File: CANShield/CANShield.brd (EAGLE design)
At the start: 53.3 x 61 mm, 31 parts, among them Q1 16MHz, U2 ARDUINO_R3_SHIELD, U4 MCP2515, U5 MCP2551, X1 DB9 Plug

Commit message: Can shield
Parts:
- removed C7: 22pF, SparkFun-Capacitors:0603-CAP
- removed CONTACTOR, CONTACTOR2, LEDS, PACKV: MSTBA2, con-phoenix-508:MSTBA2
- removed D3, D7: BAS40-04, diode:SOT23
- removed F2: PTCTHERMISTOR1206, SparkFun-PowerIC:PTC-1206
- removed S2: RESET, SparkFun-Electromechanical:TACTILE-SWITCH-SMD
- removed U2: ARDUINO_R3_SHIELD, SparkFun-Boards:UNO_R3_SHIELD
- removed U4: MCP2515, SparkFun-DigitalIC:SO-18W
- added F3: 1812L, ptc-littlefuse:1812L
- added FANS, ON: MSTBA3, con-phoenix-508:MSTBA3
- added FAN_LEDS, GAUGES_APA102, PACK_LEDS: MSTBA4, con-phoenix-508:MSTBA4
- added IC1: 7805DT, linear:TO252
- added IC2: 74LVC2G125DCT, 74xx-little-de:SSOP08
- added J2: POWERPOLE_POWER25A_HORIZONTAL_G2, powerpoles:POWERPOLE_PAIR_25A_HORIZ_G2
- added PRECHG1, PRECHG2: (no value), SparkFun-Connectors:MOLEX-1X6
- added Q2, Q3, Q4, Q5, Q6: MOSFET-NCHANNELFDD8780, SparkFun-DiscreteSemi:DPAK
- added Q7: MOSFET-NCHANNELBSS123LT1G, SparkFun-DiscreteSemi:SOT23-3
- added Q8: BSS123, transistor-small-signal:SOT23
- added R11, R15, R17, R19, R21, R23, R24, R25, R26, R27, R28, R8: 10K, SparkFun-Resistors:0603-RES
- added R14, R16, R18, R20, R6, R7, R9: 100R, SparkFun-Resistors:0603-RES
- added R22, R31, R32: (no value), SparkFun-Passives:0603-RES
- added R29: 100R, SparkFun-Passives:0603-RES
- added R30: 10K, SparkFun-Passives:0603-RES
- added R4: 100K, SparkFun-Resistors:0603-RES
- added SBO_1, SBO_2: (no value), adafruit:JST-PH-2-THM-RA
- added SG1: BUZZERNS, SparkFun-Electromechanical:BUZZER-12MM-NS
- added U$1: TEENSY_3.0_BASIC-PGM, Teensy3.0:TEENSY_3.0_BASIC-PGM
- added U$2: F6136TR-ND, ptc-littlefuse:1812L
- C1: value 0.1uF -> (none); device SparkFun-Capacitors:0603-CAP -> SparkFun-Capacitors:EIA3216
- C4: value 4.7uF -> (none); device SparkFun-Capacitors:0603-CAP -> SparkFun-Capacitors:EIA3216
- C5: value 22pF -> (none)
- D1: value MBRA140 -> (none); device SparkFun-DiscreteSemi:SMA-DIODE -> SparkFun-LED:LED-1206
- D2: value BAS40-04 -> 250mA/100V; device diode:SOT23 -> SparkFun-DiscreteSemi:SOD-323
- D5: device SparkFun-DiscreteSemi:SOT23-3 -> SparkFun-DiscreteSemi:SOT23-3@1
- F1: value (none) -> 1812L; device SparkFun-PowerIC:PTC-1206 -> ptc-littlefuse:1812L
- Q1: value 16MHz -> MOSFET-NCHANNELFDD8780; device SparkFun-FreqCtrl:CRYSTAL-SMD-5X3 -> SparkFun-DiscreteSemi:DPAK
- R1, R5: value (none) -> 10K
- R2: value 100R -> 100K
- moved D2 290.0 mm to (-132.1, -224.8), turned to 0 degrees
- moved C5 276.8 mm to (-128.3, -213.4), turned to 0 degrees
- moved D1 222.2 mm to (-90.2, -144.8), turned to 0 degrees
- moved C4 128.7 mm to (-61.0, -52.1), turned to 0 degrees
- moved C1 122.6 mm to (-62.2, -54.6), turned to 0 degrees
- moved Q1 61.3 mm to (71.1, 27.9)
- moved C3 57.2 mm to (23.5, 103.5)
- moved R12 57.2 mm to (23.5, 100.3)
- moved X1 57.2 mm to (26.7, 108.0)
- moved C2 57.1 mm to (24.8, 94.5)
- moved C6 57.1 mm to (23.7, 92.2)
- moved D5 57.1 mm to (19.1, 98.8)
- moved R1 57.1 mm to (27.9, 68.6)
- moved R10 57.1 mm to (24.8, 96.5)
- moved R13 57.1 mm to (14.6, 91.4)
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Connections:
- removed net 12V: C4.1, D1.C, U2.VIN
- removed net A0: D7.3, R2.1, U2.A0
- removed net AREF: U2.AREF
- removed net CAN_CS: U2.D10, U4.16
- removed net CAN_INT: U2.D2, U4.12
- removed net CONTACT_SENSE_1: CONTACTOR2.1, D3.3, R5.2, U2.D9
- removed net CONTACT_SENSE_2: CONTACTOR.1, D2.3, R1.2, U2.D8
- removed net D3: U2.D3
- removed net D4: U2.D4
- removed net D5: U2.D5
- removed net MISO: U2.D12, U4.15
- removed net MOSI: U2.D11, U4.14
- removed net RS: S2.3, U2.RES, U4.17
- removed net RX: U2.RX
- removed net SCK: U2.D13, U4.13
- removed net TX: U2.TX
- new net +12V: F1.2, F3.2, FANS.1, J2.RED, ON.1, PRECHG1.2, PRECHG2.2, U$2.1
- new net +5V: C1.A, C5.1, C6.2, D2.C, IC1.2, IC2.8, R22.2, SG1.+, U$1.VIN, U5.3
- new net ACTIVE_1: PRECHG1.4, R24.1, U$1.17/A3
- new net ACTIVE_2: PRECHG2.4, R27.1, U$1.14/A0
- new net BUZZER: R29.1, U$1.20/A6
- new net CHARGED_1: PRECHG1.5, R25.1, U$1.18/A4
- new net CHARGED_2: PRECHG2.5, R28.1, U$1.15/A1
- new net CHARGING_1: PRECHG1.6, R23.1, U$1.19/A5
- new net CHARGING_2: PRECHG2.6, R26.1, U$1.16/A2
- new net FANS_B: R20.1, U$1.9
- new net FANS_G: R18.1, U$1.6
- new net FANS_R: R16.1, U$1.5
- new net FAN_PWM: R31.1, U$1.10
- new net LED_C: IC2.5, U$1.13
- new net N$11: PACK_LEDS.4, Q3.4
- new net N$12: Q1.1, R7.2, R8.2
- new net N$15: Q3.1, R14.2, R15.2
- new net N$19: F3.1, FAN_LEDS.1
- new net N$20: FAN_LEDS.2, Q4.4
- new net N$21: FAN_LEDS.3, Q5.4
- new net N$22: FAN_LEDS.4, Q6.4
- new net N$23: Q4.1, R16.2, R17.2
- new net N$24: Q5.1, R18.2, R19.2
- new net N$25: Q6.1, R20.2, R21.2
- new net N$26: Q7.1, R29.2, R30.2
- new net N$27: Q8.1, R31.2, R32.2
- new net N$28: FANS.3, Q8.3
- new net N$29: GAUGES_APA102.1, U$2.2
- new net N$4: R4.2, SBO_2.1
- new net N$5: GAUGES_APA102.4, R6.1
- new net N$6: PACK_LEDS.2, Q1.4
- new net N$7: F1.1, PACK_LEDS.1
- new net N$8: PACK_LEDS.3, Q2.4
- new net PACK_B: R14.1, U$1.23/A9
- new net PACK_G: R9.1, U$1.22/A8
- new net PACK_R: R7.1, U$1.21/A7
- new net SBO_SENSE_1: R1.2, R4.1, U$1.7
- new net SBO_SENSE_2: R2.1, R5.2, U$1.8
- new net VBAT: U$1.VBAT
- new net VCC: C4.A, IC1.1, ON.2
- net 3.3V: now also U$1.3.3V, U$1.3.3V1; no longer U2.3.3V
- net 5V: now also PRECHG1.3, PRECHG2.3, R1.1, R23.2, R24.2, R25.2, R26.2, R27.2, R28.2, R5.1; no longer C1.2, C6.2, D2.2, D3.2, D7.2, F2.2, U2.5V, U4.18, U5.3
- net CAN_RXD: now also U$1.4; no longer U4.2
- net CAN_TXD: now also U$1.3; no longer U4.1
- net GND: now also C1.C, C4.C, C5.2, D1.C, FANS.2, GAUGES_APA102.2, IC1.3, IC2.1, IC2.4, IC2.7, J2.BLACK, ON.3, PRECHG1.1, PRECHG2.1, Q1.3, Q2.3, Q3.3, Q4.3, Q5.3, Q6.3, Q7.2, Q8.2, R11.1, R15.1, R17.1, R19.1, R21.1, R30.1, R32.1, R8.1, U$1.AGND, U$1.GND, U$1.GND1; no longer C1.1, C4.2, C5.1, C7.1, D2.1, D3.1, D7.1, LEDS.1, PACKV.2, R1.1, R5.1, S2.1, U2.GND@0, U2.GND@1, U2.GND@2, U4.9
- net LED_D: now also IC2.2, U$1.11; no longer R3.2, U2.SDA
- net N$1: now also SBO_1.1; no longer PACKV.1
- net N$13: now also Q2.1, R11.2, R9.2; no longer F1.2, X1.9
- net N$16: now also R22.1; no longer F1.1
- net N$17: now also IC2.6, R3.2; no longer C7.2, Q1.3, U4.8
- net N$18: now also D2.A, Q7.3, SG1.-; no longer C5.2, Q1.1, U4.7
- net N$2: now also IC2.3, R6.2; no longer CONTACTOR.2, CONTACTOR2.2, F2.1
- net N$3: now also GAUGES_APA102.3; no longer LEDS.2
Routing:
- net 5V: track 81.8 -> 0.00 mm, vias 2 -> 0
- net PACK_R: track 0.00 -> 56.9 mm
- net CONTACT_SENSE_2: track 54.5 -> 0.00 mm
- net PACK_G: track 0.00 -> 47.0 mm
- net CAN_INT: track 45.1 -> 0.00 mm, vias 1 -> 0
- net CAN_TXD: track 6.24 -> 49.7 mm
- net CONTACT_SENSE_1: track 39.5 -> 0.00 mm
- net PACK_B: track 0.00 -> 38.1 mm
- net A0: track 31.6 -> 0.00 mm, vias 1 -> 0
- net RS: track 29.7 -> 0.00 mm, vias 1 -> 0
- net CAN_RXD: track 11.3 -> 40.3 mm
- net N$2: track 23.1 -> 0.00 mm
- net SCK: track 22.4 -> 0.00 mm, vias 1 -> 0
- net MISO: track 22.4 -> 0.00 mm, vias 1 -> 0
- net MOSI: track 21.8 -> 0.00 mm, vias 1 -> 0
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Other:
- board size 53.3 x 61 mm -> 88.9 x 116.8 mm
- board text removed: "Units: inches"

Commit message: Most of the base board finished
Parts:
- removed PRECHG1, PRECHG2: (no value), SparkFun-Connectors:MOLEX-1X6
- removed R23, R24, R25, R26, R27, R28: 10K, SparkFun-Resistors:0603-RES
- removed SBO_1, SBO_2: (no value), adafruit:JST-PH-2-THM-RA
- added D3, D4: BAS40-04, diode:SOT23
- added H1, H2, H3, H4: MOUNT-PAD-ROUND3.0, holes:3,0-PAD
- added IC3, IC4, IC5: ILD213T, SparkFun-DiscreteSemi:SO08
- added SBO_LOOP_1, SBO_LOOP_2: MSTBA2, con-phoenix-508:MSTBA2
- C1, C4: device SparkFun-Capacitors:EIA3216 -> SparkFun-Capacitors:PANASONIC_C
- moved R32 386.9 mm to (69.8, 82.5)
- moved R31 386.9 mm to (69.8, 85.1)
- moved Q8 384.7 mm to (74.9, 85.1), turned to 270 degrees
- moved D2 360.7 mm to (64.8, 77.5), turned to 270 degrees
- moved R29 359.1 mm to (61.8, 71.1)
- moved R30 359.1 mm to (61.8, 68.6)
- moved Q7 358.2 mm to (66.0, 71.1), turned to 270 degrees
- moved SG1 355.1 mm to (72.4, 75.4)
- moved C5 341.9 mm to (72.4, 63.5)
- moved R22 303.8 mm to (91.4, 95.2), turned to 180 degrees
- moved D1 302.5 mm to (88.9, 99.1)
- moved R21 223.8 mm to (61.0, 22.9)
- moved C1 213.9 mm to (83.8, 101.6), turned to 180 degrees
- moved IC1 206.9 mm to (76.2, 109.2)
- moved C4 204.9 mm to (68.6, 106.7)
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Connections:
- net +12V: no longer PRECHG1.2, PRECHG2.2
- net +5V: now also C1.+; no longer C1.A
- net 5V: now also D3.2, D4.2; no longer PRECHG1.3, PRECHG2.3, R23.2, R24.2, R25.2, R26.2, R27.2, R28.2
- net ACTIVE_1: no longer PRECHG1.4, R24.1
- net ACTIVE_2: no longer PRECHG2.4, R27.1
- net BUZZER: now also U$1.23/A9; no longer U$1.20/A6
- net CHARGED_1: no longer PRECHG1.5, R25.1
- net CHARGED_2: no longer PRECHG2.5, R28.1
- net CHARGING_1: no longer PRECHG1.6, R23.1
- net CHARGING_2: no longer PRECHG2.6, R26.1
- net FANS_B: now also U$1.5; no longer U$1.9
- net FANS_R: now also U$1.9; no longer U$1.5
- net GND: now also C1.-, C4.-, D3.1, D4.1, H1.B3,0, H2.B3,0, H3.B3,0, H4.B3,0, SBO_LOOP_1.2, SBO_LOOP_2.2; no longer C1.C, C4.C, PRECHG1.1, PRECHG2.1
- net N$1: now also SBO_LOOP_2.1; no longer SBO_1.1
- net N$4: now also SBO_LOOP_1.1; no longer SBO_2.1
- net PACK_B: now also U$1.22/A8; no longer U$1.23/A9
- net PACK_G: now also U$1.21/A7; no longer U$1.22/A8
- net PACK_R: now also U$1.20/A6; no longer U$1.21/A7
- net SBO_SENSE_1: now also D3.3
- net SBO_SENSE_2: now also D4.3
- net VCC: now also C4.+; no longer C4.A
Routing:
- net +5V: track 0.00 -> 137.1 mm
- net FANS_R: track 0.00 -> 105.7 mm, vias 0 -> 1
- net FANS_G: track 0.00 -> 96.0 mm, vias 0 -> 1
- net FANS_B: track 0.00 -> 85.1 mm, vias 0 -> 1
- net LED_D: track 0.00 -> 72.6 mm, vias 0 -> 1
- net LED_C: track 0.00 -> 57.3 mm, vias 0 -> 1
- net CHARGING_1: track 0.00 -> 29.8 mm
- net VCC: track 0.00 -> 28.6 mm
- net CHARGED_1: track 0.00 -> 26.8 mm
- net ACTIVE_1: track 0.00 -> 23.7 mm
- net +12V: track 0.00 -> 21.4 mm
- net CHARGING_2: track 0.00 -> 20.6 mm
- net CHARGED_2: track 0.00 -> 17.6 mm
- net BUZZER: track 0.00 -> 17.1 mm
- net SBO_SENSE_1: track 0.00 -> 16.4 mm
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- added copper zone on layer 16, net +12V
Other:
- board size 88.9 x 116.8 mm -> 96.5 x 128.3 mm
- board text removed: "RESET"

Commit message: precharge progress
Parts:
- removed IC4, IC5: ILD213T, SparkFun-DiscreteSemi:SO08
- added 74HC125M: MM74HC125M, Fairchild_By_element14_Batch_1:SOIC127P600X175-14N
- added D10, D11, D6, D7: (no value), SparkFun-DiscreteSemi:SOD-123
- added LM393M: LM393M, Fairchild_By_element14_Batch_1:SOIC127P600X180-8N
- added PRECHARGE_FUSE: FUSEX20MM, SparkFun-Passives:FUSE_5MM
- added PRECHARGE_RELAY, PRECHARGE_RELAY1: DS2Y-S-DC5V, relay:DS2Y
- added Q11, Q13, Q14, Q9: IRLML6344TRPBF, SparkFun-DiscreteSemi:SOT23
- added R23, R24, R25, R26: 10K, SparkFun-Passives:0603-RES
- added R33, R45: 100k, SparkFun-Resistors:0603-RES
- added R34, R41, R46, R47: 10k, SparkFun-Resistors:0603-RES
- added R36, R37, R42: 470k, SparkFun-Resistors:0805
- added R38, R43: 13K, SparkFun-Resistors:0805
- added R39: 110k, SparkFun-Resistors:0805
- added R40: 12K, SparkFun-Resistors:0805
- added U$4: (no value), prosthesis:PROS_LOGO
- added U$5: REE-0505S, grant:REE-0505S
- added U$7, U$8: RELAY-2G5Q, SparkFun-Electromechanical:RELAY-G5V
- added X2, X3, X4, X5: SMKDSP_1,5/2, con-phoenix-smkdsp:SMKDSP_1,5/2
- FANS, ON: value MSTBA3 -> SMKDSP_1,5/3; device con-phoenix-508:MSTBA3 -> con-phoenix-smkdsp:SMKDSP_1,5/3
- FAN_LEDS, GAUGES_APA102, PACK_LEDS: value MSTBA4 -> SMKDSP_1,5/4; device con-phoenix-508:MSTBA4 -> con-phoenix-smkdsp:SMKDSP_1,5/4
- Q7: device SparkFun-DiscreteSemi:SOT23-3 -> SparkFun-DiscreteSemi:SOT23
- R10, R12, R13: device SparkFun-Resistors:0603-RES -> SparkFun-Resistors:0603-RES@1
- SBO_LOOP_1, SBO_LOOP_2: value MSTBA2 -> SMKDSP_1,5/2; device con-phoenix-508:MSTBA2 -> con-phoenix-smkdsp:SMKDSP_1,5/2
- moved Q7 46.0 mm to (44.5, 111.8), turned to 0 degrees
- moved R30 45.3 mm to (41.1, 108.8), turned to 270 degrees
- moved R29 40.9 mm to (44.1, 108.0), turned to 180 degrees
- moved D1 39.6 mm to (62.2, 69.8)
- moved SG1 39.2 mm to (53.0, 109.5), turned to 270 degrees
- moved R22 37.1 mm to (62.2, 72.4), turned to 0 degrees
- moved IC1 33.6 mm to (69.8, 76.2), turned to 180 degrees
- moved D2 32.3 mm to (58.9, 109.2), turned to 90 degrees
- moved C1 31.4 mm to (62.2, 78.7), turned to 0 degrees
- moved C4 29.3 mm to (77.5, 78.7), turned to 180 degrees
- moved ON 20.9 mm to (76.2, 109.2)
- moved D4 19.1 mm to (57.1, 6.60), turned to 270 degrees
- moved SBO_LOOP_1 19.1 mm to (80.0, -8.89)
- moved SBO_LOOP_2 19.1 mm to (66.0, -8.89)
- moved IC3 18.3 mm to (26.7, 55.9)
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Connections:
- removed net CHARGED_1: U$1.18/A4
- removed net CHARGING_1: U$1.19/A5
- new net 96V_IN_FUSED: PRECHARGE_FUSE.1, PRECHARGE_RELAY.8, PRECHARGE_RELAY1.8, R37.2
- new net CAP_CHARGE_REF: LM393M.2, R39.1, R40.2
- new net CAP_CHARGE_V_CURR_1: LM393M.3, R36.1, R38.2
- new net CAP_CHARGE_V_CURR_2: R42.1, R43.2
- new net CHARGE_1: IC3.6, R23.1, U$1.19/A5
- new net CHARGE_2: IC3.8, R26.1, U$1.18/A4
- new net CHARGE_ISO_1: 74HC125M.3, R25.2
- new net CHARGE_ISO_2: 74HC125M.6, R24.2
- new net CONTACT_EN_1: Q13.1, R46.1
- new net CONTACT_EN_2: Q14.1, R47.1
- new net GNDI: IC3.2, IC3.4, U$5.-VOUT, X4.2
- new net N$30: R37.1, R39.2
- new net N$31: 74HC125M.12, 74HC125M.9, LM393M.7, R45.2
- new net N$32: IC3.3, R25.1
- new net N$33: D10.A, Q14.3, U$8.9
- new net N$34: IC3.1, R24.1
- new net N$35: D11.A, Q13.3, U$7.9
- new net N$36: 74HC125M.8
- new net N$37: 74HC125M.11
- new net N$38: U$7.5, U$7.6
- new net N$39: U$8.5, U$8.6
- new net N$40: PRECHARGE_RELAY.13, X2.1
- new net N$41: PRECHARGE_RELAY1.13, X3.1
- new net N$42: PRECHARGE_FUSE.3, X4.1
- new net PRECHARGE_EN_1: Q9.1, R34.1
- new net PRECHARGE_EN_2: Q11.1, R41.1
- new net PRECHARGE_OUT_1: PRECHARGE_RELAY.6, PRECHARGE_RELAY.9, R36.2, X5.1
- new net PRECHARGE_OUT_2: PRECHARGE_RELAY1.6, PRECHARGE_RELAY1.9, R42.2, X5.2
- new net PRECHARGE_RESISTOR_IN: PRECHARGE_RELAY.4, X2.2
- new net PRECHARGE_RESISTOR_IN1: PRECHARGE_RELAY1.4, X3.2
- new net PRECH_DRAIN: D6.A, PRECHARGE_RELAY.16, Q9.3
- new net PRECH_DRAIN1: D7.A, PRECHARGE_RELAY1.16, Q11.3
- new net PRECH_STATE_TO_BUFF: 74HC125M.2, 74HC125M.5, LM393M.1, R33.2
- net +12V: now also D10.C, D11.C, U$7.2, U$8.2
- net +5V: now also R23.2, R26.2, U$5.+VIN
- net 5V: now also 74HC125M.14, D6.C, D7.C, LM393M.8, PRECHARGE_RELAY.1, PRECHARGE_RELAY1.1, R33.1, R45.1, U$5.+VOUT
- net BUZZER: now also U$1.10; no longer U$1.23/A9
- net FAN_PWM: now also U$1.23/A9; no longer U$1.10
- net GND: now also 74HC125M.1, 74HC125M.10, 74HC125M.13, 74HC125M.4, 74HC125M.7, IC3.5, IC3.7, LM393M.4, PRECHARGE_RELAY.11, PRECHARGE_RELAY1.11, Q11.2, Q13.2, Q14.2, Q9.2, R34.2, R38.1, R40.1, R41.2, R43.1, R46.2, R47.2, U$5.-VIN, U$7.10, U$8.10
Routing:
- net VCC: track 28.6 -> 137.9 mm, vias 0 -> 2
- net SBO_SENSE_2: track 3.13 -> 109.4 mm, vias 0 -> 2
- net SBO_SENSE_1: track 16.4 -> 110.2 mm, vias 0 -> 2
- net +5V: track 137.1 -> 182.0 mm, vias 0 -> 1
- net CHARGE_1: track 0.00 -> 44.1 mm
- net CHARGE_2: track 0.00 -> 44.0 mm
- net PRECHARGE_OUT_1: track 0.00 -> 39.0 mm
- net 96V_IN_FUSED: track 0.00 -> 37.5 mm
- net ACTIVE_2: track 14.5 -> 45.0 mm
- net CHARGING_1: track 29.8 -> 0.00 mm
- net CHARGED_1: track 26.8 -> 0.00 mm
- net CHARGED_2: track 17.6 -> 40.7 mm
- net PRECHARGE_OUT_2: track 0.00 -> 22.7 mm
- net PRECHARGE_RESISTOR_IN1: track 0.00 -> 21.1 mm
- net PRECHARGE_RESISTOR_IN: track 0.00 -> 21.1 mm
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- added copper zone on layer 1, net GNDI
- added copper zone on layer 16, net GNDI
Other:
- board size 96.5 x 128.3 mm -> 114.3 x 133.3 mm
- board text added: "Pack Controller Rev. 1"

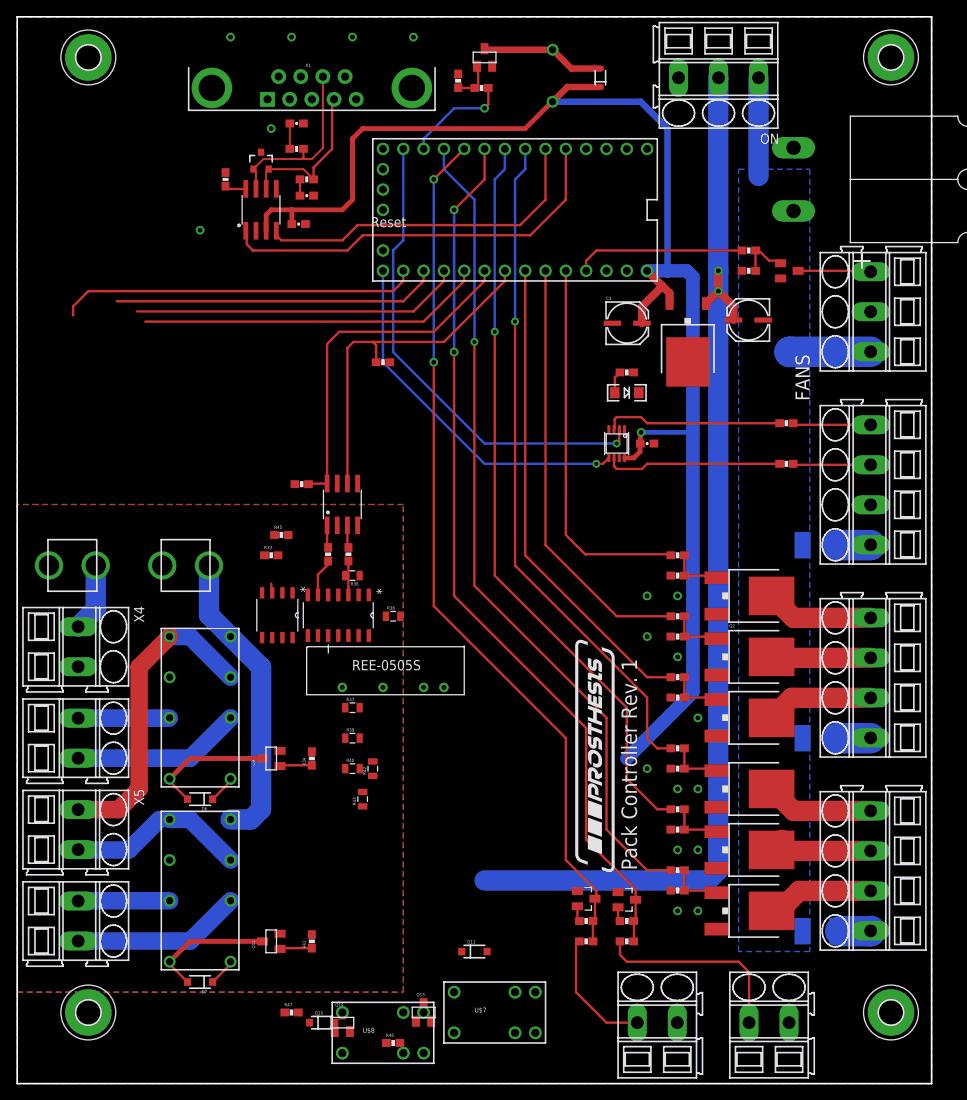
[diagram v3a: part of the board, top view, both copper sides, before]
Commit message: down to one airwire
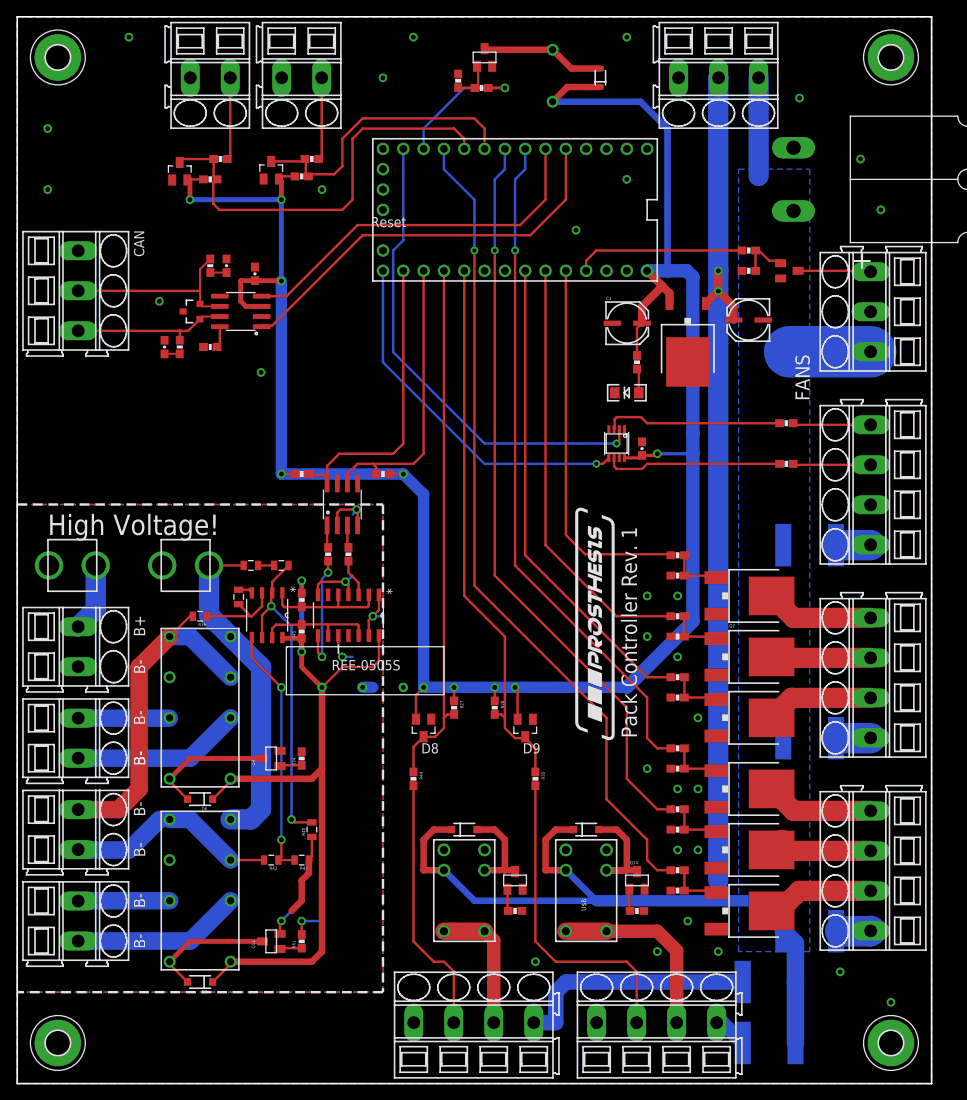
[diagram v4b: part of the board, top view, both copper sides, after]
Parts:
- removed X1: DB9 Plug, SparkFun-Connectors:DB9_MALE
- added CAN: SMKDSP_1,5/3, con-phoenix-smkdsp:SMKDSP_1,5/3
- added CONTACTOR_1, CONTACTOR_2: SMKDSP_1,5/4, con-phoenix-smkdsp:SMKDSP_1,5/4
- added D8, D9: BAS40-04, diode:SOT23
- added PF1, PF2: PTC-2920L, polyswitch:2920L
- added R27, R28: 10K, SparkFun-Resistors:0603-RES
- added R35, R44: 100K, SparkFun-Resistors:0603-RES
- F1, F3: value 1812L -> PTC-2920L; device ptc-littlefuse:1812L -> polyswitch:2920L
- U$2: device ptc-littlefuse:1812L -> polyswitch:2920L
- moved SBO_LOOP_1 131.8 mm to (21.6, 109.2), turned to 180 degrees
- moved SBO_LOOP_2 130.7 mm to (10.2, 109.2), turned to 180 degrees
- moved R2 108.0 mm to (11.4, 99.1), turned to 0 degrees
- moved R4 105.4 mm to (22.9, 99.1), turned to 0 degrees
- moved D4 104.2 mm to (6.35, 97.5), turned to 0 degrees
- moved R5 103.9 mm to (10.2, 96.5)
- moved R1 101.6 mm to (21.6, 96.9)
- moved D3 101.4 mm to (17.8, 97.7), turned to 0 degrees
- moved R47 45.0 mm to (63.5, 5.08)
- moved D10 40.9 mm to (57.1, 15.2)
- moved Q14 40.9 mm to (63.5, 8.89)
- moved C3 32.5 mm to (4.45, 75.6), turned to 270 degrees
- moved U$8 31.0 mm to (57.1, 7.62), turned to 90 degrees
- moved R12 28.8 mm to (6.35, 75.6), turned to 90 degrees
- moved R39 23.3 mm to (19.1, 48.3), turned to 180 degrees
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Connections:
- removed net ACTIVE_1: U$1.17/A3
- removed net ACTIVE_2: U$1.14/A0
- removed net CHARGED_2: U$1.15/A1
- removed net CHARGING_2: U$1.16/A2
- removed net GNDI: IC3.2, IC3.4, U$5.-VOUT, X4.2
- removed net N$36: 74HC125M.8
- removed net N$37: 74HC125M.11
- removed net NC1: X1.1
- removed net NC2: X1.4
- removed net NC3: X1.6
- removed net NC5: X1.8
- new net AGND: 74HC125M.1, 74HC125M.10, 74HC125M.13, 74HC125M.4, 74HC125M.7, IC3.2, IC3.4, LM393M.4, PRECHARGE_RELAY.11, PRECHARGE_RELAY1.11, Q11.2, Q9.2, R34.2, R38.1, R40.1, R41.2, R43.1, U$5.-VOUT, X4.2
- new net CONTACTOR_CLOSED_SENSE_1: D8.3, R27.2, R44.1, U$1.16/A2
- new net CONTACTOR_CLOSED_SENSE_2: D9.3, R28.2, R35.1, U$1.17/A3
- new net N$43: CONTACTOR_1.4, PF2.2
- new net N$44: CONTACTOR_2.4, PF1.2
- new net N$45: CONTACTOR_2.2, R35.2
- new net N$46: CONTACTOR_1.2, R44.2
- net +12V: now also PF1.1, PF2.1
- net +5V: now also D3.2, D4.2, D8.2, D9.2, R1.1, R27.1, R28.1, R5.1
- net 5V: no longer D3.2, D4.2, R1.1, R5.1
- net CAP_CHARGE_REF: now also LM393M.6
- net CAP_CHARGE_V_CURR_2: now also LM393M.5
- net CHARGE_1: now also U$1.15/A1; no longer U$1.19/A5
- net CHARGE_2: now also U$1.14/A0; no longer U$1.18/A4
- net CHARGE_ISO_2: now also 74HC125M.8; no longer 74HC125M.6
- net GND: now also CAN.1, CONTACTOR_1.1, CONTACTOR_2.1, D8.1, D9.1; no longer 74HC125M.1, 74HC125M.10, 74HC125M.13, 74HC125M.4, 74HC125M.7, LM393M.4, PRECHARGE_RELAY.11, PRECHARGE_RELAY1.11, Q11.2, Q9.2, R34.2, R38.1, R40.1, R41.2, R43.1, X1.3
- net N$38: now also CONTACTOR_1.3
- net N$39: now also CONTACTOR_2.3
- net PIN2: now also CAN.2; no longer X1.2
- net PIN7: now also CAN.3; no longer X1.7
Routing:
- net +5V: track 182.0 -> 274.6 mm, vias 1 -> 9
- net 5V: track 10.7 -> 95.6 mm, vias 0 -> 2
- net +12V: track 22.5 -> 102.9 mm
- net SBO_SENSE_1: track 110.2 -> 37.2 mm, vias 2 -> 0
- net CONTACTOR_CLOSED_SENSE_2: track 0.00 -> 68.9 mm
- net CONTACTOR_CLOSED_SENSE_1: track 0.00 -> 66.5 mm
- net SBO_SENSE_2: track 109.4 -> 52.5 mm, vias 2 -> 0
- net AGND: track 0.00 -> 47.5 mm, vias 0 -> 6
- net ACTIVE_2: track 45.0 -> 0.00 mm
- net ACTIVE_1: track 43.3 -> 0.00 mm
- net CHARGING_2: track 41.2 -> 0.00 mm
- net CAP_CHARGE_REF: track 0.00 -> 40.8 mm, vias 0 -> 2
- net CHARGED_2: track 40.7 -> 0.00 mm
- net N$45: track 0.00 -> 40.1 mm
- net N$46: track 0.00 -> 32.5 mm
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- added copper zone on layer 1, net AGND
- added copper zone on layer 16, net AGND
- removed copper zone on layer 1, net GNDI
- removed copper zone on layer 16, net GNDI
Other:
- board text added: "B+"
- board text added: "B-"
- board text added: "High Voltage!"
